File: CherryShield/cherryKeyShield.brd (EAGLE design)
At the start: 100 x 80 mm, 19 parts

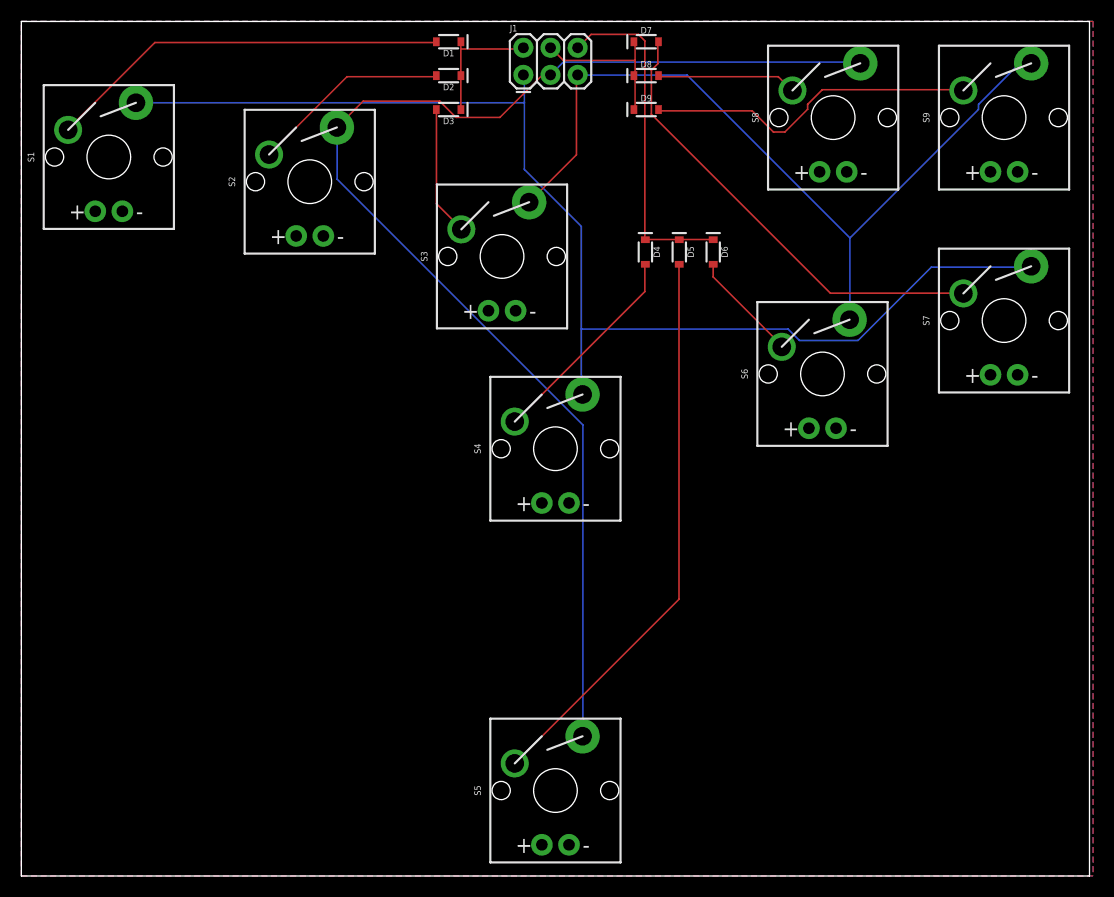
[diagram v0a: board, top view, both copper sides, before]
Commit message: minimized size for cost
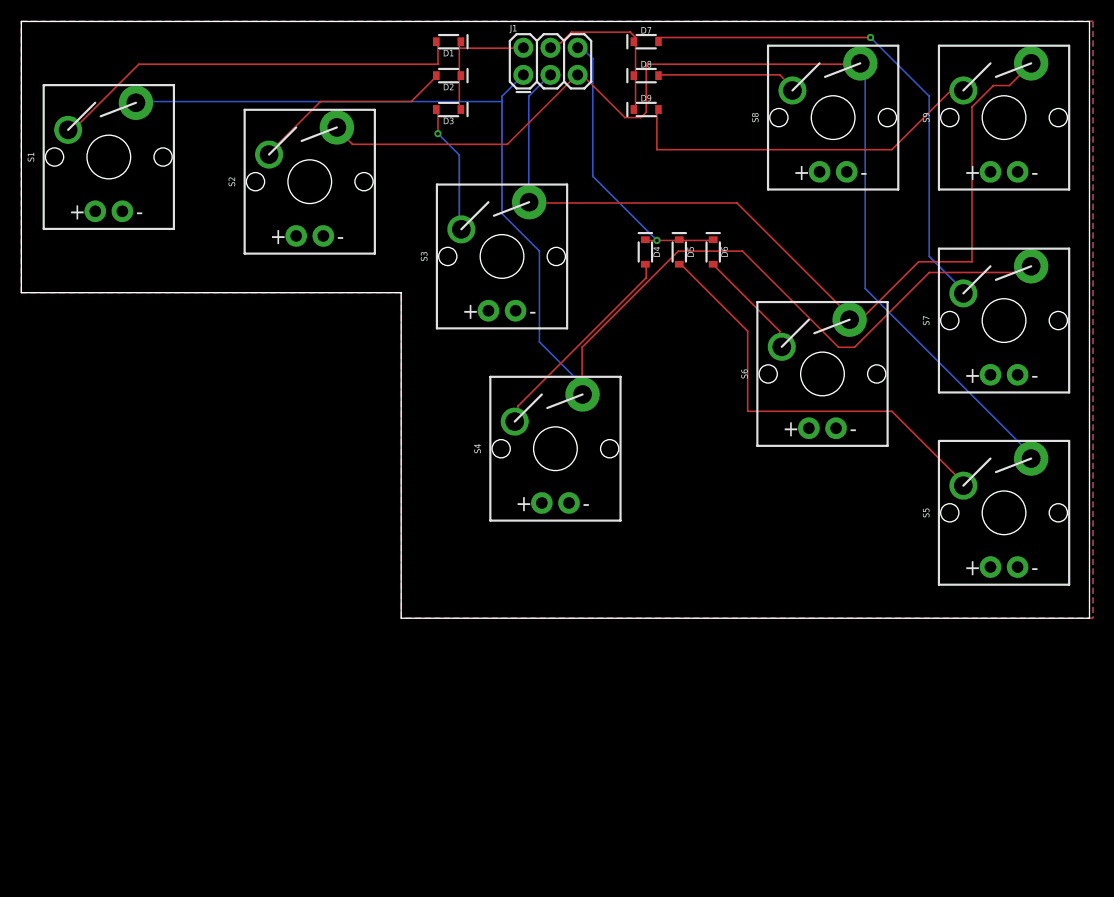
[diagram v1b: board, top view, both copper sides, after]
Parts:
- moved S5 49.4 mm to (92.0, 34.0)
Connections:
- net X1: now also J1.5; no longer J1.3
- net X2: now also J1.3; no longer J1.5
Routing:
- net X1: track 119.4 -> 102.7 mm
- net N$1: track 53.1 -> 39.7 mm
- net X0: track 114.1 -> 125.2 mm
- net X2: track 77.3 -> 83.0 mm
- net N$14: track 43.2 -> 47.9 mm, vias 0 -> 1
- net Y1: track 32.1 -> 27.7 mm, vias 0 -> 1
- net N$17: track 31.4 -> 34.8 mm
- net N$7: track 37.9 -> 39.4 mm
- net Y2: track 15.0 -> 15.8 mm
- net N$11: track 12.2 -> 12.1 mm, vias 0 -> 1
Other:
- board size 100 x 80 mm -> 100 x 55.9 mm
